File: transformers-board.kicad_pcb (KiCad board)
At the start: 2 copper layers, 50 parts, among them J1 Screw_Terminal_01x02, J2 Screw_Terminal_01x02, J3 Screw_Terminal_01x02, Q1 IRF3205, U1 UC2844NG4, U2 PC47PQ20_16Z-22

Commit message: Add layout updates
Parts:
- moved C10 126.9 mm to (189.2, 122.5), turned to 270 degrees
- moved C8 124.5 mm to (204.2, 122.7), turned to 270 degrees
- moved C9 122.8 mm to (204.2, 105.2), turned to 90 degrees
- moved C22 116.6 mm to (79.8, 121.7), turned to 270 degrees
- moved D4 115.1 mm to (174.2, 117.9), turned to 90 degrees
- moved U2 113.6 mm to (150.9, 126.5), turned to 90 degrees
- moved C7 105.5 mm to (213.4, 121.2), turned to 90 degrees
- moved C13 104.2 mm to (165.4, 129.5)
- moved C11 103.0 mm to (189.2, 105.1), turned to 90 degrees
- moved R8 101.6 mm to (166.9, 119.1)
- moved R12 97.6 mm to (62.5, 116.1), turned to 270 degrees
- moved C6 93.4 mm to (213.6, 106.4), turned to 270 degrees
- moved R10 92.6 mm to (161.3, 110.8), turned to 270 degrees
- moved D8 89.6 mm to (62.5, 97.8), turned to 90 degrees
- moved D5 88.1 mm to (162.8, 126.5)
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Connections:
- C21 pad 1: GNDA -> VCCQ
- C21 pad 2: VCCQ -> GNDA
- C23 pad 1: GNDA -> VCCQ
- C23 pad 2: VCCQ -> GNDA
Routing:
- net VCC: track 0.00 -> 127.3 mm, vias 0 -> 2
- net GNDA: track 0.00 -> 55.7 mm, vias 0 -> 4
- net Net-(C10-Pad1): track 0.00 -> 48.0 mm
- net Net-(C14-Pad1): track 0.00 -> 42.3 mm
- net Net-(C15-Pad2): track 0.00 -> 35.8 mm, vias 0 -> 1
- net +5V: track 0.00 -> 33.8 mm
- net VCCQ: track 0.00 -> 28.5 mm
- net Net-(C4-Pad1): track 0.00 -> 25.9 mm, vias 0 -> 2
- net Net-(Q1-Pad1): track 0.00 -> 25.3 mm
- net Net-(D2-Pad2): track 0.00 -> 16.6 mm
- net Net-(C12-Pad1): track 0.00 -> 16.3 mm
- net Net-(D5-Pad2): track 0.00 -> 10.3 mm
- net Net-(C5-Pad1): track 0.00 -> 10.3 mm
- net Net-(D7-Pad2): track 0.00 -> 6.86 mm
- net Net-(C15-Pad1): track 0.00 -> 3.32 mm
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- added copper zone on F.Cu, net GND
- added copper zone on B.Cu, net GNDA
- added copper zone on F.Cu, net Net-(C10-Pad1)
- added copper zone on F.Cu, net VCCQ
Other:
- board outline added: 168.1 x 91.9 mm
- board text added: "CC1310-01 Sparsh Bansal"

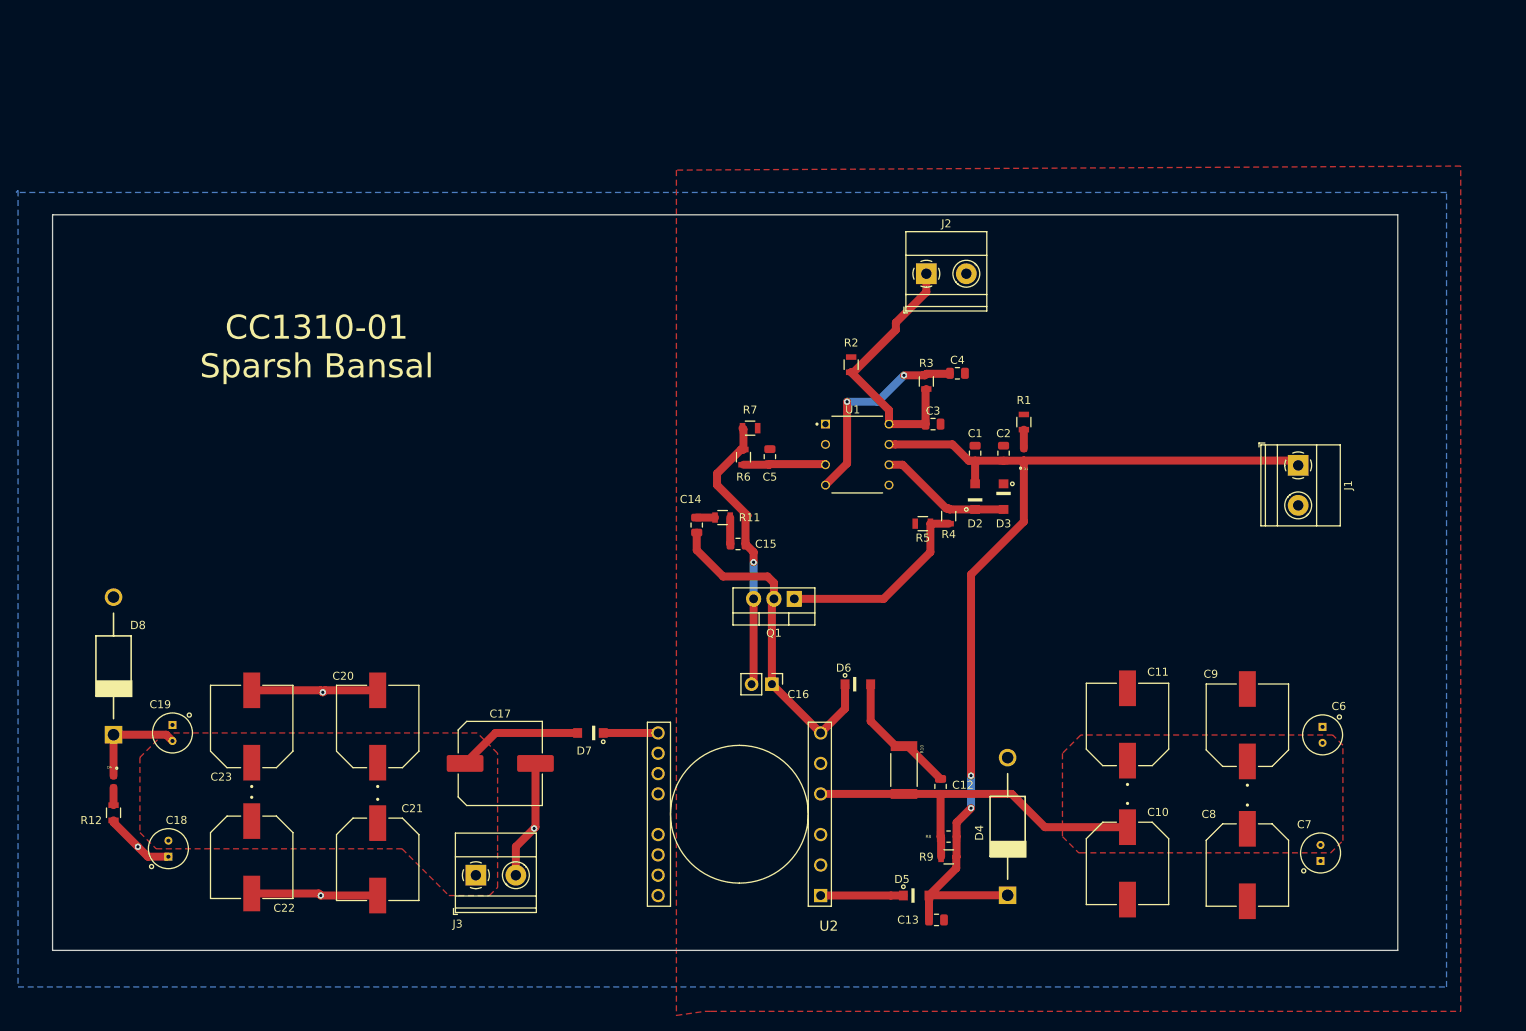
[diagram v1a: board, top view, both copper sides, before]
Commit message: Make changes for Beat's comments
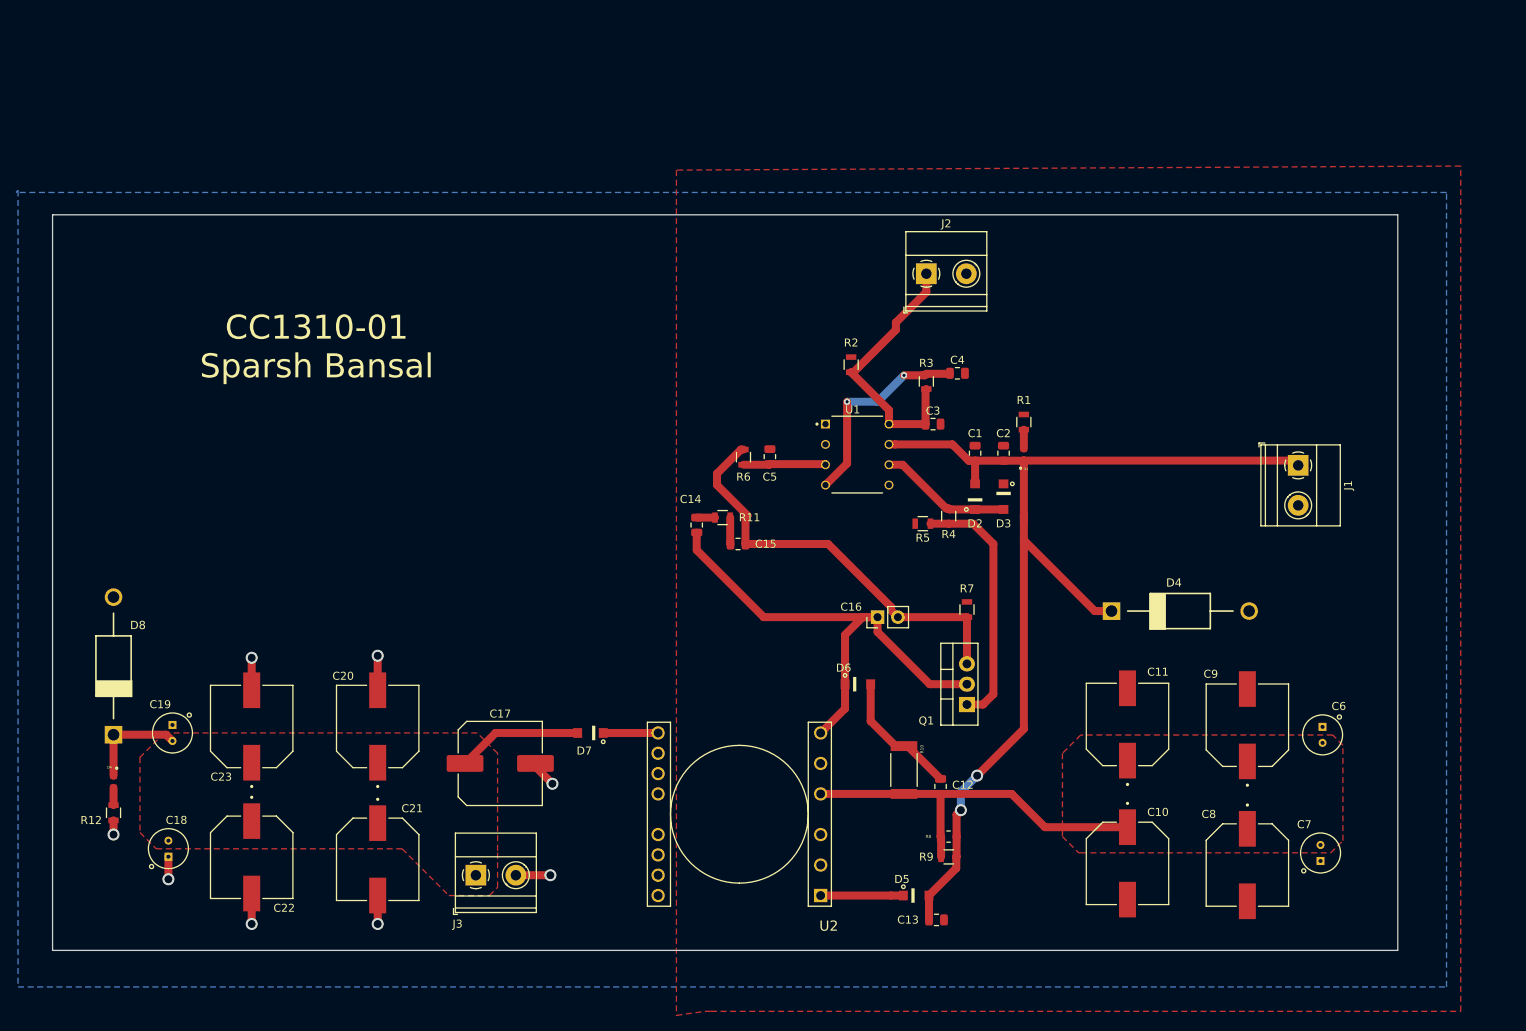
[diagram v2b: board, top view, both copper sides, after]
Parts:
- D2, D3, D5, D6, D7: value SL04-E3-08 -> SS2FL4-M3/H
- R7: value 0.75 -> 0.05
- moved R7 35.3 mm to (169.2, 90.7), turned to 270 degrees
- moved D4 34.5 mm to (195.8, 90.9), turned to 0 degrees
- moved Q1 25.3 mm to (169.2, 102.6), turned to 90 degrees
- moved C16 15.6 mm to (158.0, 91.7), turned to 90 degrees
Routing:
- net GNDA: track 55.7 -> 28.1 mm, vias 4 -> 8
- net Net-(C14-Pad1): track 42.3 -> 62.5 mm
- net Net-(C15-Pad2): track 35.8 -> 52.6 mm, vias 1 -> 0
- net Net-(Q1-Pad1): track 25.3 -> 31.5 mm
- net VCC: track 127.3 -> 132.9 mm

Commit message: Add fabrication outputs
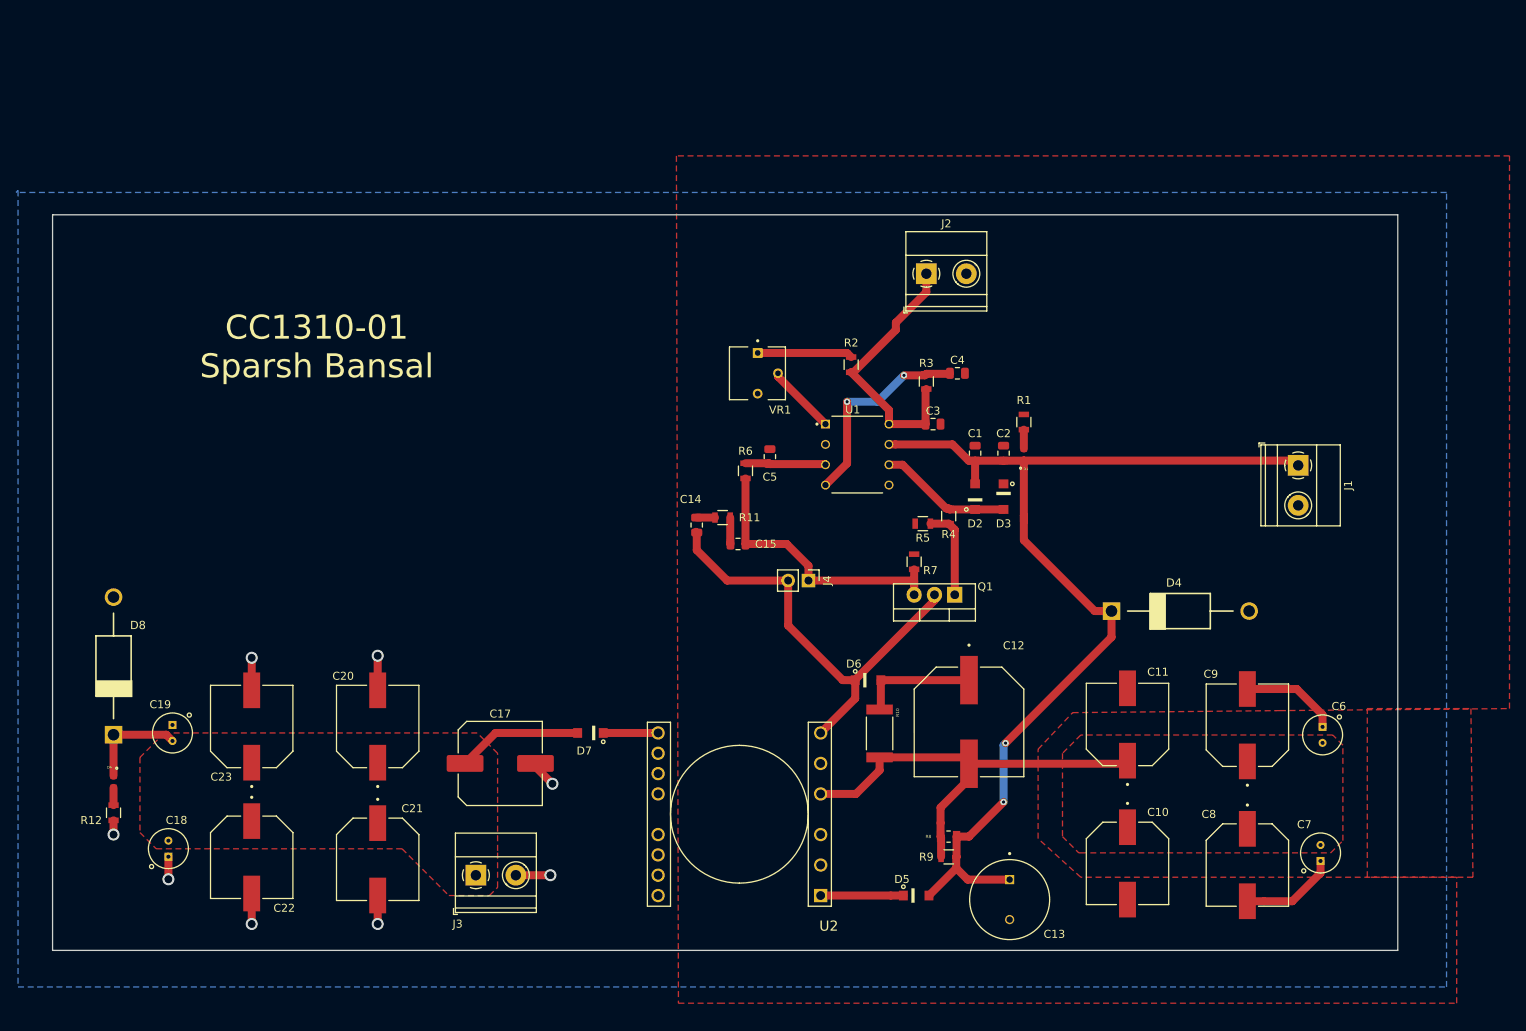
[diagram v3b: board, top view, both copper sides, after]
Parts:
- removed C16: 1.014nF (DO NOT POPULATE - TEST POINT), Connector_PinHeader_2.54mm:PinHeader_1x02_P2.54mm_Vertical
- added J4: Conn_01x02_Male, Connector_PinHeader_2.54mm:PinHeader_1x02_P2.54mm_Vertical, F.Cu at (149.4, 87.1)
- added VR1: 3362P-1-102LF, transformers-board:TRIM_3362P-1-102LF, F.Cu at (143.0, 61.2)
- C12: footprint Capacitor_SMD:C_0805_2012Metric -> transformers-board:CAPAE1350X1400N
- C13: footprint Capacitor_SMD:C_0805_2012Metric -> transformers-board:CAPPRD500W60D1000H1800
- moved Q1 13.8 mm to (167.6, 88.9), turned to 180 degrees
- moved C13 9.49 mm to (174.5, 127.0), turned to 270 degrees
- moved R7 8.91 mm to (162.6, 84.8)
- moved C12 8.81 mm to (169.4, 104.8)
- moved R10 5.49 mm to (158.2, 106.2)
- moved R6 1.73 mm to (141.5, 73.4), turned to 270 degrees
- moved D6 1.37 mm to (156.8, 99.6)
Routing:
- net GND: track 0.00 -> 24.3 mm
- net Net-(Q1-Pad1): track 31.5 -> 11.5 mm
- net Net-(C15-Pad2): track 52.6 -> 37.2 mm
- net Net-(R2-Pad2): track 0.00 -> 11.9 mm
- net Net-(U1-Pad1): track 0.00 -> 8.81 mm
- net Net-(C14-Pad1): track 62.5 -> 55.3 mm
- net Net-(C10-Pad1): track 48.0 -> 54.8 mm
- net VCC: track 132.9 -> 133.7 mm
